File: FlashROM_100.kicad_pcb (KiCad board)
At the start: 2 copper layers, 16.5 x 34.3 mm, 7 parts, among them J1 LH535618 DIP LEGS, U1 29F010

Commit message: kicad 6
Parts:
- JP1: value ~CS~ breakout -> ~{CS} breakout
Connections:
- net /ALE_~WE renamed /ALE_~{WE}
- net /~CS renamed /~{CS}
- net /~CS_BUS renamed /~{CS_BUS}
- net /~OE renamed /~{OE}
- net /~WE renamed /~{WE}
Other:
- net class Default removed
- board text added: "Connect ~{CS} OUT to REX TP1. Leave ~{CS} IN unconnected."
- board text added: "If REX is later removed, connect ~{CS} OUT to ~{CS} IN."
- board text added: "Install a shunt on ~{CS}, or, install wires as above,"
- board text added: "Run 2 wires from ~{CS} IN & ~{CS} OUT to Option ROM compartment."
- board text added: "~{CS}"
- board text removed: "Connect ~CS~ OUT to REX TP1. Leave ~CS~ IN unconnected."
- board text removed: "If REX is later removed, connect ~CS~ OUT to ~CS~ IN."
- board text removed: "Install a shunt on ~CS~, or, install wires as above,"
- board text removed: "Run 2 wires from ~CS~ IN & ~CS~ OUT to Option ROM compartment."
- board text removed: "~CS"

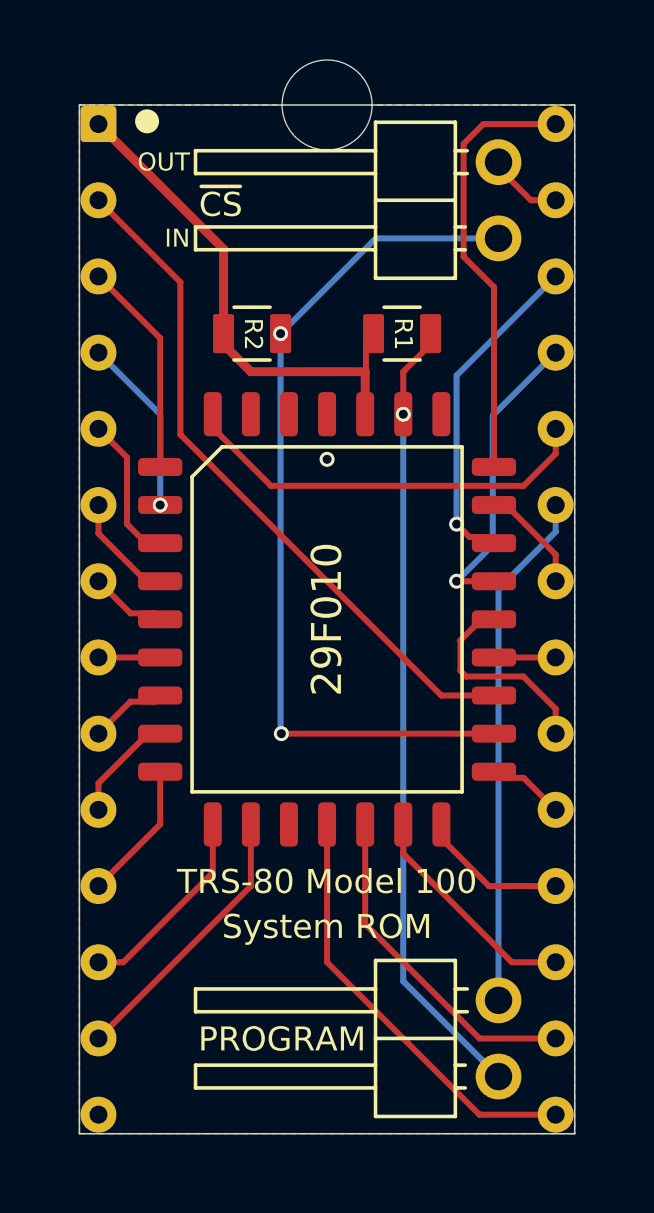
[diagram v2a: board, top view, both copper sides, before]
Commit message: Fix wrong pinout on FlashROM_100 TSOPgit add -A!
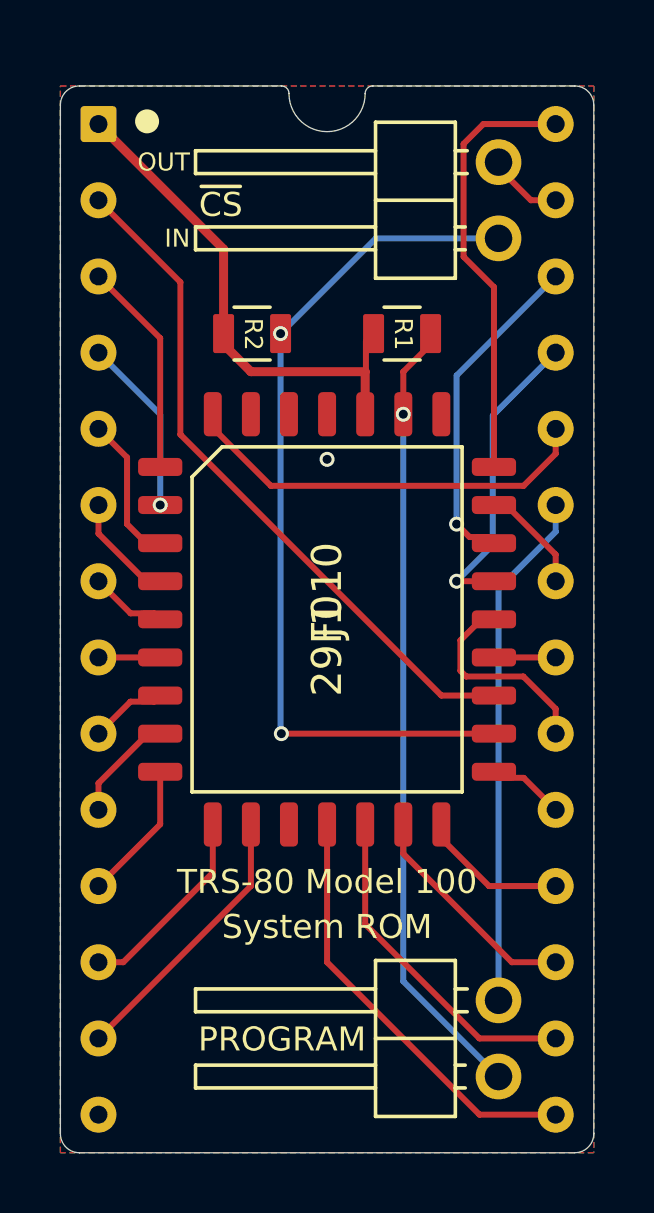
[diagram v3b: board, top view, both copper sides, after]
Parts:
- removed REF**: NPTH_3mm, 000_LOCAL:NPTH_3mm
- J1: footprint 000_LOCAL:DIP28_0.6_pcb_sil_pins -> 000_LOCAL:DIP28_0.6_pcb
- JP2: renamed from JP1; value ~{CS} breakout -> ~CS~ breakout
- renumbered JP2 to JP1
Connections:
- U1 pad 1: (no net) -> unconnected-(U1-Pad1)
- U1 pad 30: (no net) -> unconnected-(U1-Pad30)
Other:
- board size 16.5 x 34.3 mm -> 17.8 x 35.6 mm
